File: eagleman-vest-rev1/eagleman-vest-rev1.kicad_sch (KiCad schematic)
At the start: 27 parts, among them P1 USB_C_Plug_USB2.0, U1 ESP32-S3-WROOM-2, U2 AP1117-33

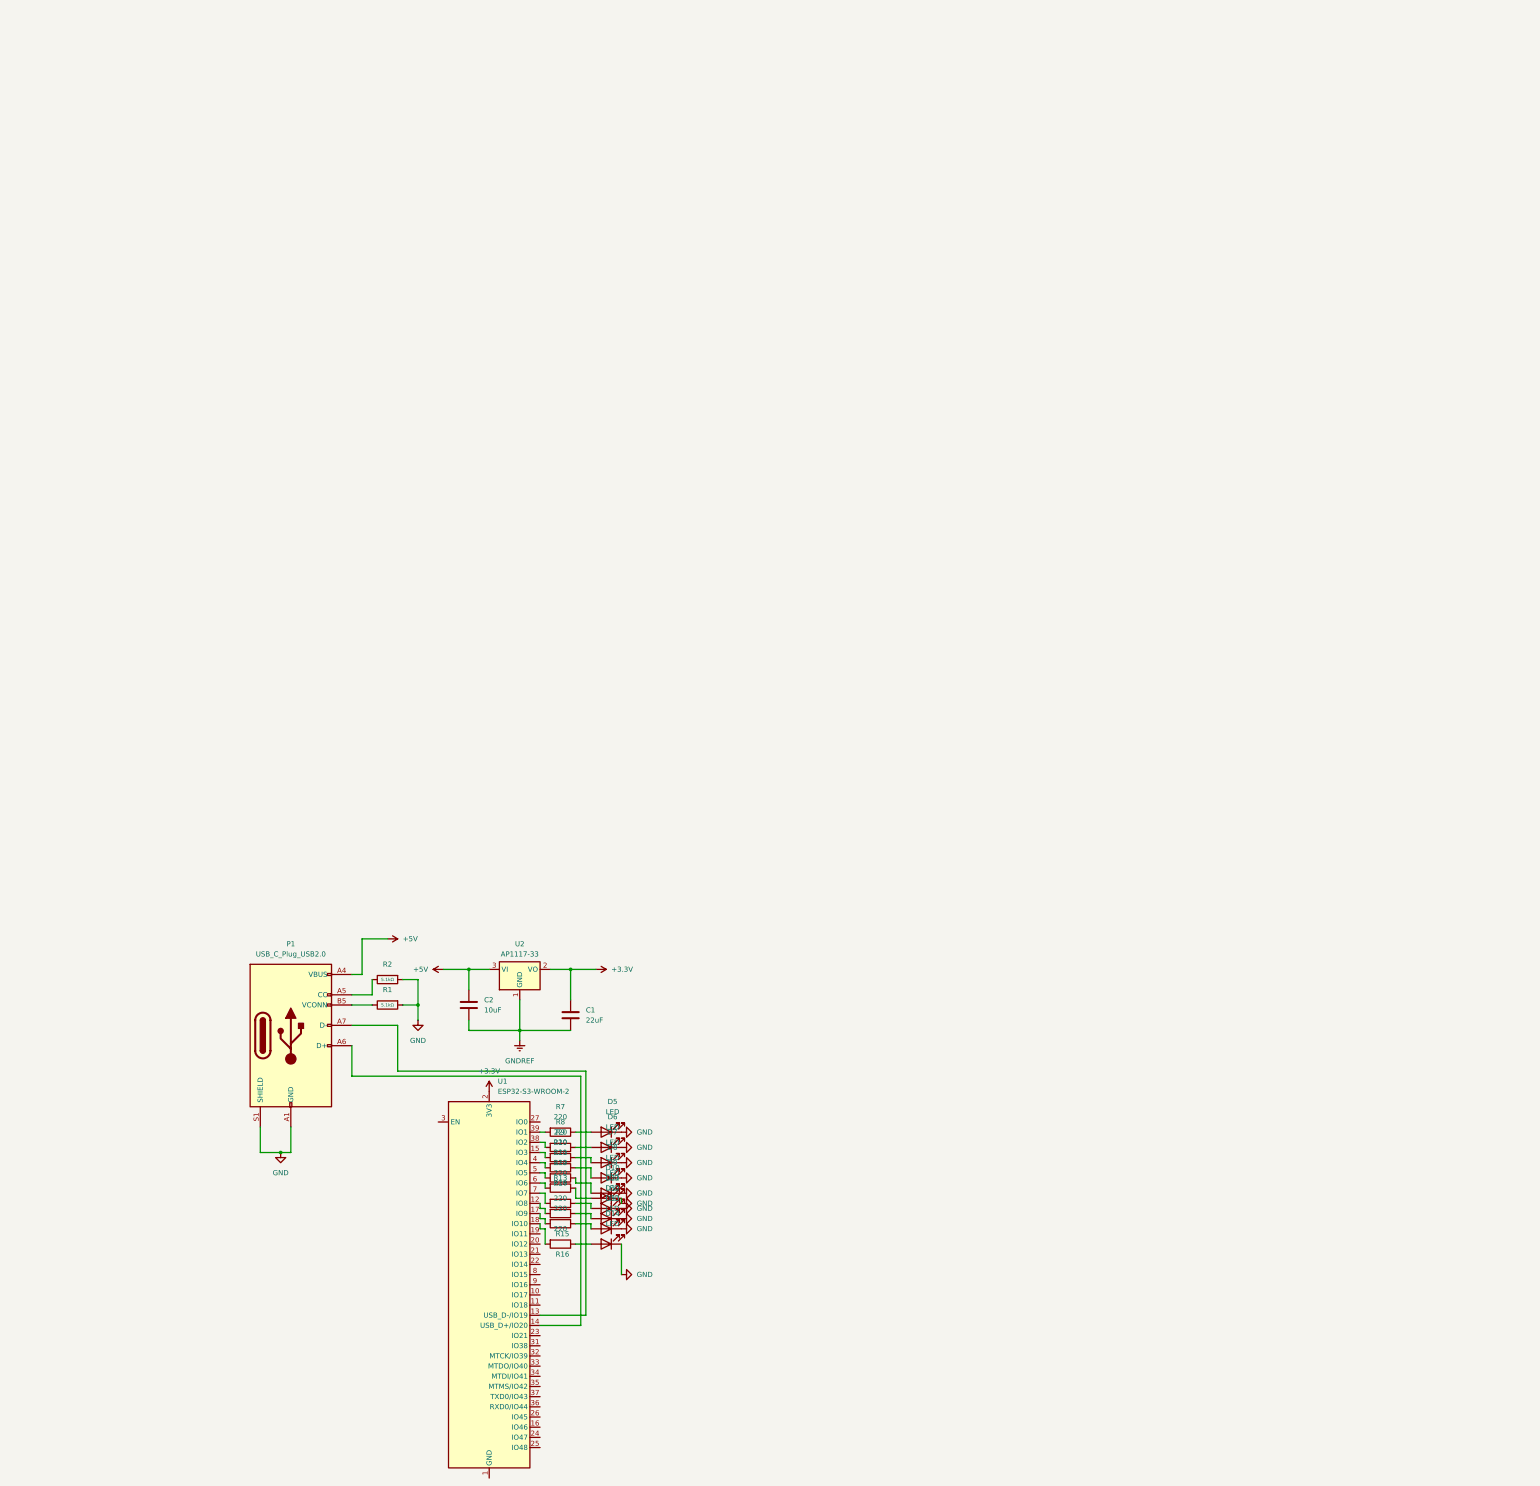
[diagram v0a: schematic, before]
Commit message: starting to fix wiring w netlabels
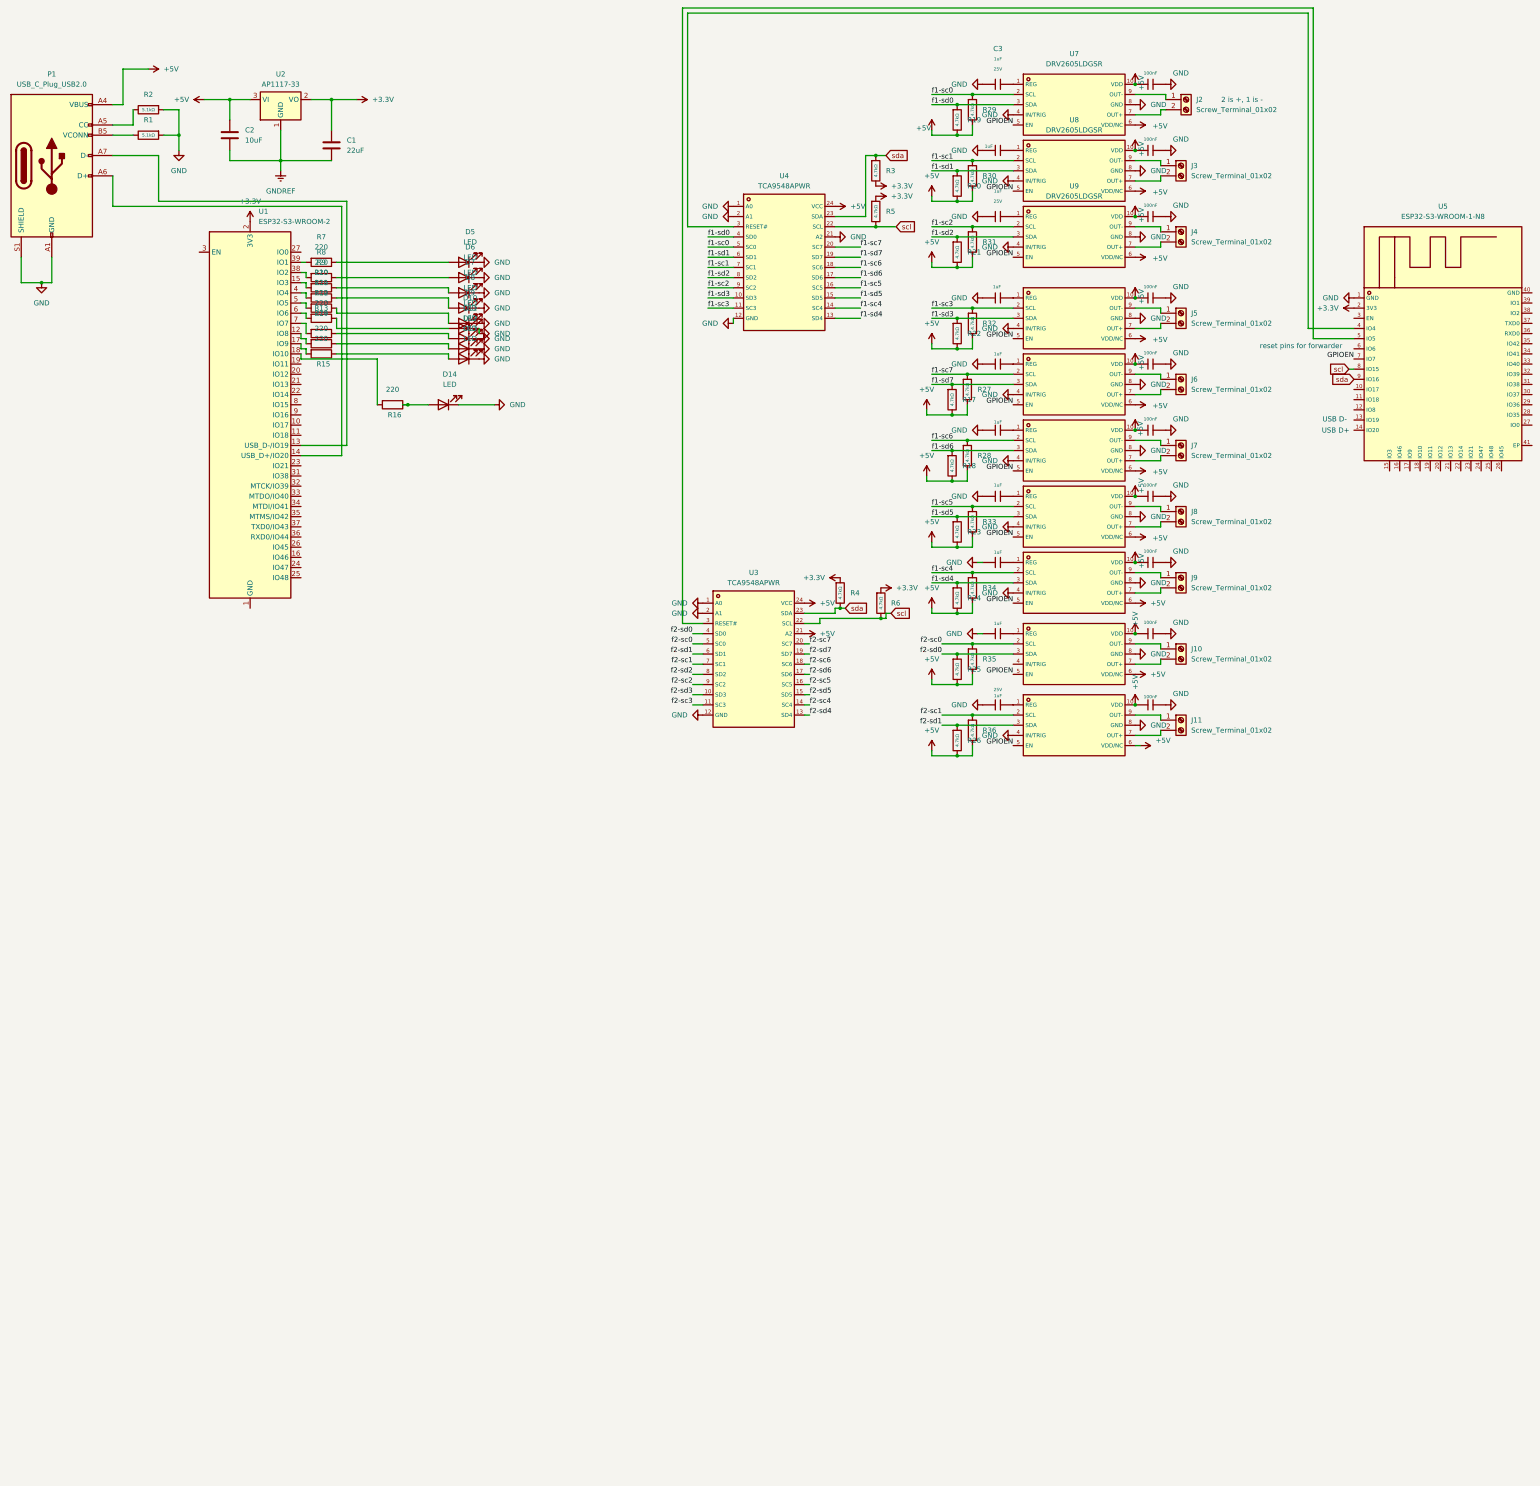
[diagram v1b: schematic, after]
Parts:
- added C10, C11, C12, C3, C4, C5, C6, C7, C8, C9: 1uF, PCM_JLCPCB:C_0402, symbol PCM_JLCPCB-Capacitors:0402,1uF
- added C13, C24, C25, C27, C29, C30, C32, C33, C35, C36: 100nF, PCM_JLCPCB:C_0402, symbol PCM_JLCPCB-Capacitors:0402,100nF
- added J10, J11, J2, J3, J4, J5, J6, J7, J8, J9: Screw_Terminal_01x02, symbol Connector:Screw_Terminal_01x02
- added R17, R18, R19, R20, R21, R22, R23, R24, R25, R26, R27, R28, R29, R3, R30, R31, R32, R33, R34, R35, R36, R4, R5, R6: 4.7kΩ, PCM_JLCPCB:R_0402, symbol PCM_JLCPCB-Resistors:0402,4.7kΩ
- added U10, U11, U12, U13, U14, U15, U16, U7, U8, U9: DRV2605LDGSR, TCA9548APWR:driver_footprint_maybe, symbol DRV2605LDGSR:DRV2605LDGSR
- added U3, U4: TCA9548APWR, TCA9548APWR:TSSOP-24_L7.8-W4.4-P0.65-LS6.4-BL, symbol i2C mux:TCA9548APWR
- added U5: ESP32-S3-WROOM-1-N8, TCA9548APWR:WIFIM-SMD_ESP32-S3-WROOM-1-N8, symbol ESP32-S3-WROOM-1-N8:ESP32-S3-WROOM-1-N8
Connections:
- net +3.3V: now also R3.2, R4.1, R5.1, R6.1, U5.2 (3V3)
- net +5V: now also C13.2, C24.2, C25.2, C27.2, C29.2, C30.2, C32.2, C33.2, C35.2, C36.2, R17.2, R18.2, R19.2, R20.2, R21.2, R22.2, R23.2, R24.2, R25.2, R26.2, R27.2, R28.2, R29.2, R30.2, R31.2, R32.2, R33.2, R34.2, R35.2, R36.2, U10.10 (VDD), U10.6 (VDD/NC), U11.10 (VDD), U11.6 (VDD/NC), U12.10 (VDD), U12.6 (VDD/NC), U13.10 (VDD), U13.6 (VDD/NC), U14.10 (VDD), U14.6 (VDD/NC), U15.10 (VDD), U15.6 (VDD/NC), U16.10 (VDD), U16.6 (VDD/NC), U3.21 (A2), U3.24 (VCC), U4.24 (VCC), U7.10 (VDD), U7.6 (VDD/NC), U8.10 (VDD), U8.6 (VDD/NC), U9.10 (VDD), U9.6 (VDD/NC)
- net GND: now also C10.2, C11.2, C12.2, C13.1, C24.1, C25.1, C27.1, C29.1, C3.2, C30.1, C32.1, C33.1, C35.1, C36.1, C4.2, C5.2, C6.2, C7.2, C8.2, C9.2, U10.4 (IN/TRIG), U10.8 (GND), U11.4 (IN/TRIG), U11.8 (GND), U12.4 (IN/TRIG), U12.8 (GND), U13.4 (IN/TRIG), U13.8 (GND), U14.4 (IN/TRIG), U14.8 (GND), U15.8 (GND), U16.4 (IN/TRIG), U16.8 (GND), U3.1 (A0), U3.12 (GND), U3.2 (A1), U4.1 (A0), U4.12 (GND), U4.2 (A1), U4.21 (A2), U5.1 (GND), U7.4 (IN/TRIG), U7.8 (GND), U8.4 (IN/TRIG), U8.8 (GND), U9.4 (IN/TRIG), U9.8 (GND)
- new net: C12.1, U16.1 (REG)
- new net: J9.1 (Pin_1), U14.9 (OUT-)
- new net: J9.2 (Pin_2), U14.7 (OUT+)
- new net: C5.1, U9.1 (REG)
- new net: C11.1, U15.1 (REG)
- new net: J11.1 (Pin_1), U16.9 (OUT-)
- new net: J11.2 (Pin_2), U16.7 (OUT+)
- new net: U4.3 (RESET#), U5.4 (IO4)
- new net: J5.1 (Pin_1), U10.9 (OUT-)
- new net: J5.2 (Pin_2), U10.7 (OUT+)
- new net: J8.1 (Pin_1), U13.9 (OUT-)
- new net: J8.2 (Pin_2), U13.7 (OUT+)
- new net: C10.1, U14.1 (REG)
- new net: C3.1, U7.1 (REG)
- new net: U3.3 (RESET#), U5.5 (IO5)
- new net: J4.2 (Pin_2), U9.7 (OUT+)
- new net: J4.1 (Pin_1), U9.9 (OUT-)
- new net: J6.1 (Pin_1), U11.9 (OUT-)
- new net: J6.2 (Pin_2), U11.7 (OUT+)
- new net: C4.1, U8.1 (REG)
- new net: J3.2 (Pin_2), U8.7 (OUT+)
- new net: J3.1 (Pin_1), U8.9 (OUT-)
- new net: C9.1, U13.1 (REG)
- new net: C7.1, U11.1 (REG)
- new net: J10.2 (Pin_2), U15.7 (OUT+)
- new net: J10.1 (Pin_1), U15.9 (OUT-)
- new net: J7.1 (Pin_1), U12.9 (OUT-)
- new net: J7.2 (Pin_2), U12.7 (OUT+)
- new net: J2.2 (Pin_2), U7.7 (OUT+)
- new net: J2.1 (Pin_1), U7.9 (OUT-)
- new net: C8.1, U12.1 (REG)
- new net: C6.1, U10.1 (REG)
- new net GPIOEN: U10.5 (EN), U11.5 (EN), U12.5 (EN), U13.5 (EN), U14.5 (EN), U15.5 (EN), U16.5 (EN), U5.7 (IO7), U7.5 (EN), U8.5 (EN), U9.5 (EN)
- new net f1-sc0: R29.1, U4.5 (SC0), U7.2 (SCL)
- new net f1-sc1: R30.1, U4.7 (SC1), U8.2 (SCL)
- new net f1-sc2: R31.1, U4.9 (SC2), U9.2 (SCL)
- new net f1-sc3: R32.1, U10.2 (SCL), U4.11 (SC3)
- new net f1-sc4: R34.1, U14.2 (SCL), U4.14 (SC4)
- new net f1-sc5: R33.1, U13.2 (SCL), U4.16 (SC5)
- new net f1-sc6: R28.1, U12.2 (SCL), U4.18 (SC6)
- new net f1-sc7: R27.1, U11.2 (SCL), U4.20 (SC7)
- new net f1-sd0: R19.1, U4.4 (SD0), U7.3 (SDA)
- new net f1-sd1: R20.1, U4.6 (SD1), U8.3 (SDA)
- new net f1-sd2: R21.1, U4.8 (SD2), U9.3 (SDA)
- new net f1-sd3: R22.1, U10.3 (SDA), U4.10 (SD3)
- new net f1-sd4: R24.1, U14.3 (SDA), U4.13 (SD4)
- new net f1-sd5: R23.1, U13.3 (SDA), U4.15 (SD5)
- new net f1-sd6: R18.1, U12.3 (SDA), U4.17 (SD6)
- new net f1-sd7: R17.1, U11.3 (SDA), U4.19 (SD7)
- new net f2-sc0: R35.1, U15.2 (SCL), U3.5 (SC0)
- new net f2-sc1: R36.1, U16.2 (SCL), U3.7 (SC1)
- new net f2-sc2: U3.9 (SC2)
- new net f2-sc3: U3.11 (SC3)
- new net f2-sc4: U3.14 (SC4)
- new net f2-sc5: U3.16 (SC5)
- new net f2-sc6: U3.18 (SC6)
- new net f2-sc7: U3.20 (SC7)
- new net f2-sd0: R25.1, U15.3 (SDA), U3.4 (SD0)
- new net f2-sd1: R26.1, U16.3 (SDA), U3.6 (SD1)
- new net f2-sd2: U3.8 (SD2)
- new net f2-sd3: U3.10 (SD3)
- new net f2-sd4: U3.13 (SD4)
- new net f2-sd5: U3.15 (SD5)
- new net f2-sd6: U3.17 (SD6)
- new net f2-sd7: U3.19 (SD7)
- new net scl: R5.2, R6.2, U3.22 (SCL), U4.22 (SCL), U5.8 (IO15)
- new net sda: R3.1, R4.2, U3.23 (SDA), U4.23 (SDA), U5.9 (IO16)
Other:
- note added: "2 is +, 1 is -"
- note added: "USB D+"
- note added: "USB D-"
- note added: "reset pins for forwarder"
- moved on the sheet: C1, C2, D10, D11, D12, D13, D14, D5, D6, D7, D8, D9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

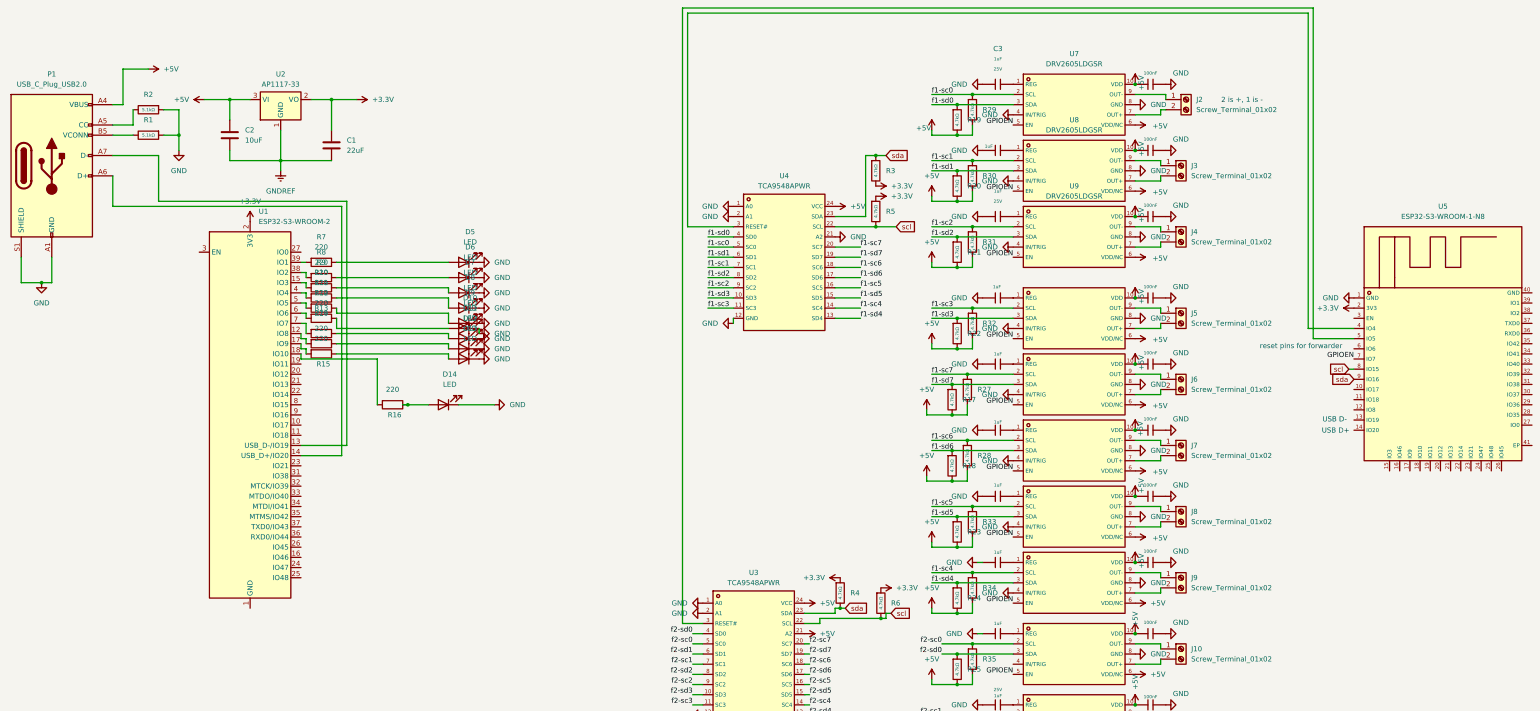
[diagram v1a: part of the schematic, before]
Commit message: removed duplicate esp32 - why is its footprint not gone?
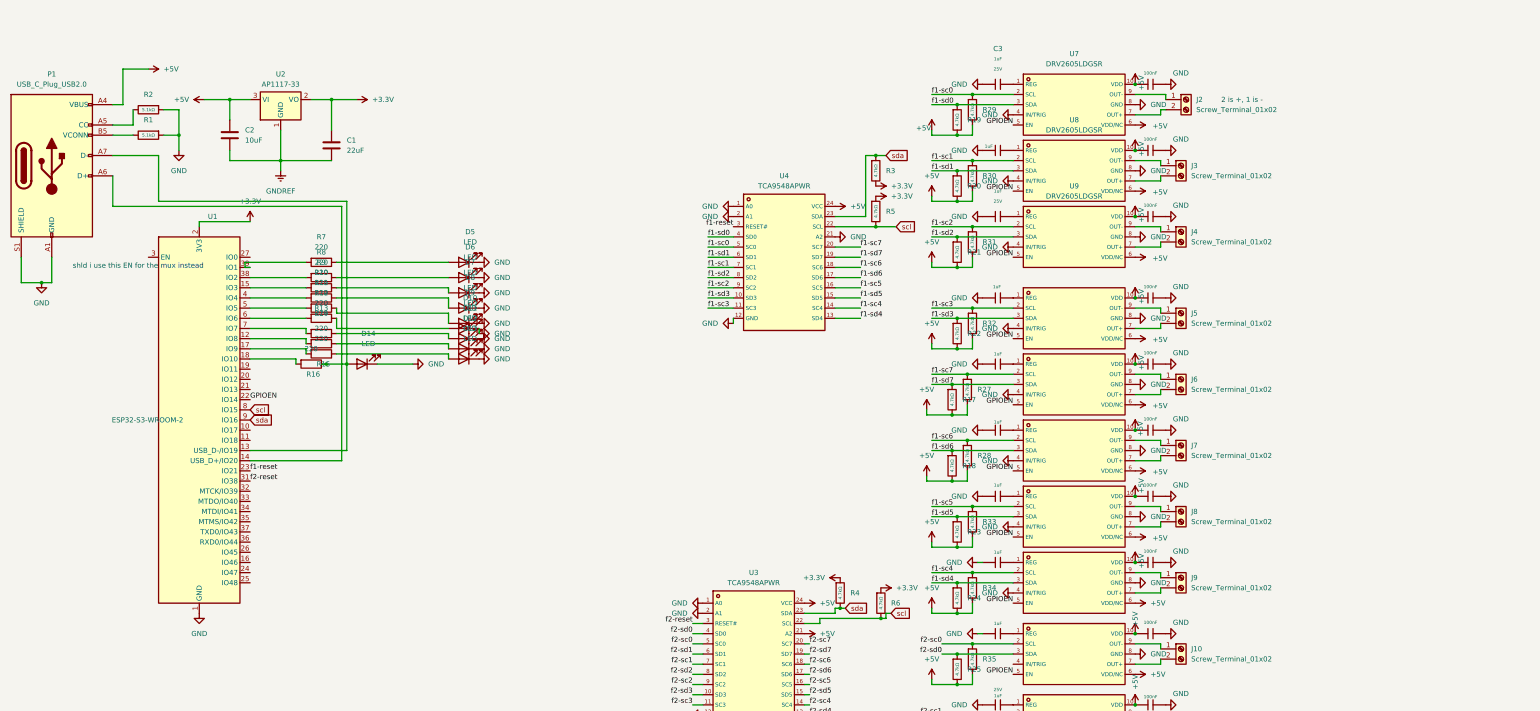
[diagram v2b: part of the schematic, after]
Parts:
- removed U5: ESP32-S3-WROOM-1-N8, TCA9548APWR:WIFIM-SMD_ESP32-S3-WROOM-1-N8, symbol ESP32-S3-WROOM-1-N8:ESP32-S3-WROOM-1-N8
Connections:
- net GND: now also U1.1 (GND), U1.40 (GND), U1.41 (GND)
- net GPIOEN: now also U1.22 (IO14)
- net scl: now also U1.8 (IO15)
- net sda: now also U1.9 (IO16)
- net f1-reset: now reaches U4.3 (RESET#)
- net f1-reset: now also U1.23 (IO21)
- net at P1.A7 (D-), U1.13 (USB_D-/IO19): now also D14.2 (A), R16.1
- net f2-reset: now reaches U3.3 (RESET#)
- net f2-reset: now also U1.31 (IO38)
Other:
- note added: "shld i use this EN for the mux instead"
- note removed: "USB D+"
- note removed: "USB D-"
- note removed: "reset pins for forwarder"
- moved on the sheet: D14, R16, U1
